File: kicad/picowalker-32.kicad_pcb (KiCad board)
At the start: 2 copper layers, 44.1 x 51 mm, 50 parts, among them IC1 TFBS4711-TT1, J1 DBG_HDR, J2 PROGRAM_HDR, J5 USB_C_Receptacle_USB2.0, SW1 SW_Push, SW2 SW_Push, SW3 SW_Push, SW5 BOOTSEL, U1 MCP73871, U10 MCP1700x-180xxTT, U11 USBLC6-2P6, U12 STM32U535CET6-modified, U2 M95512-DWDW4TP_K, U3 BMA400, U4 W25Q128JVS

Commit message: Change schematic MCU pinouts
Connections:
- U12 pad 10: TXDIR -> WKUP
- U12 pad 11: RXDIR -> ACCEL_INT1
- U12 pad 12: SCREEN_CSB -> DBG_TX
- U12 pad 14: SOUND_SRC -> SCREEN_CSB
- U12 pad 15: unconnected-(U12-PA5-Pad15) -> SOUND_SRC
- U12 pad 20: WKUP -> SCREEN_RST
- U12 pad 21: unconnected-(U12-PB10-Pad21) -> DBG_RX
- U12 pad 25: unconnected-(U12-PB12-Pad25) -> TP_INT
- U12 pad 30: DBG_TX -> TXDIR
- U12 pad 31: DBG_RX -> RXDIR
- U12 pad 39: SWO -> BSTAT2
- U12 pad 45: /stm32u5/~{BAT_LO} -> ~{PG}
- U12 pad 46: unconnected-(U12-PB9-Pad46) -> BSTAT1

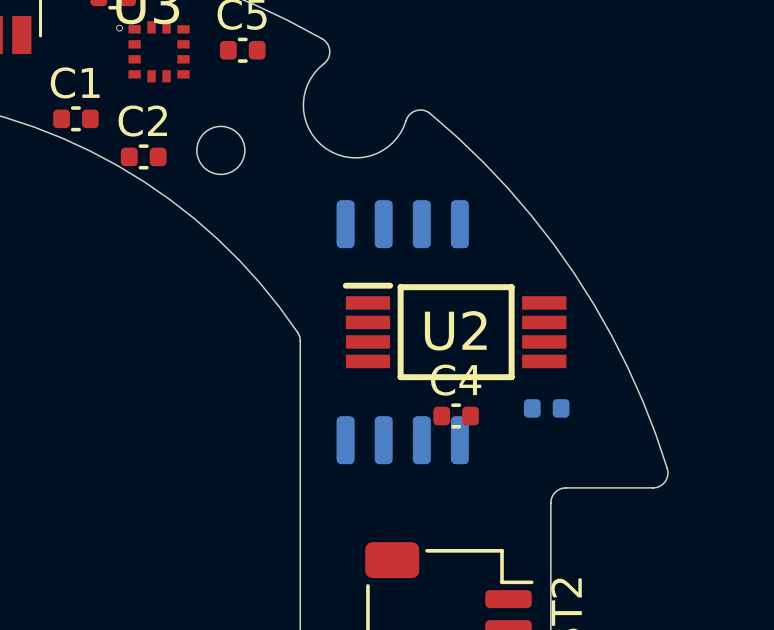
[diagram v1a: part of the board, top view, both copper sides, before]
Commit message: comments about power, changed eeprom and flash packages
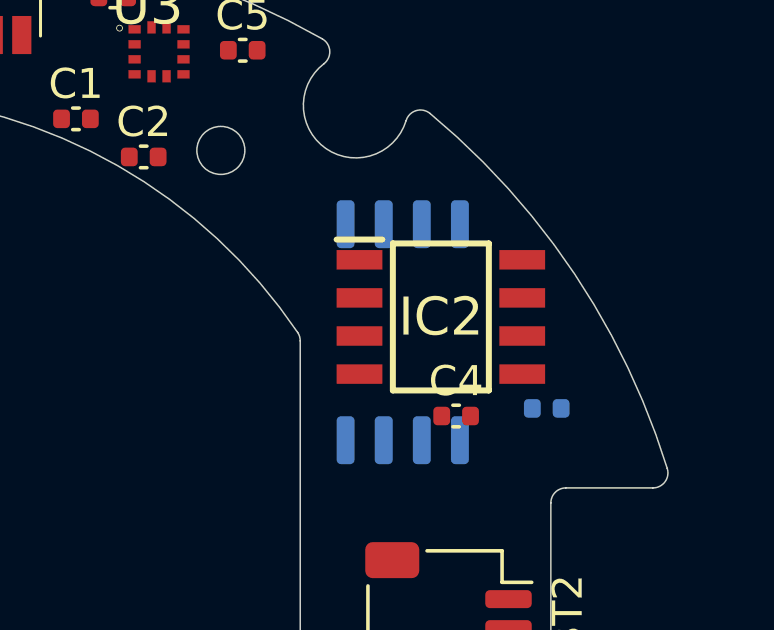
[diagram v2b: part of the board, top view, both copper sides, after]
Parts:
- removed U2: M95512-DWDW4TP_K, Samacsys_Parts:SOP65P640X120-8N
- added IC2: M95512-DRMN8TP_K, SamacSys_Parts:SOIC127P600X175-8N, F.Cu at (116.3, 68.8)
- C26: value C -> 4.7uF
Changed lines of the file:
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@@
         (effects (font (size 1 1) (thickness 0.15)))
     )
-    (fp_text value "C" (at 0 1.16) (layer "F.Fab")
+    (fp_text value "4.7uF" (at 0 1.16) (layer "F.Fab")
         (effects (font (size 1 1) (thickness 0.15)))
     )
@@
     )
   )
-  (footprint "Samacsys_Parts:SOP65P640X120-8N" (layer "F.Cu")
-    (at 116.84 69.342)
-    (descr "M95512-DWDW4TP/K")
-    (tags "Integrated Circuit")
-    (property "Description" "Automotive 512 Kbit SPI bus EEPROM with high speed clock")
-    (property "Height" "1.2")
-    (property "Manufacturer_Name" "STMicroelectronics")
-    (property "Manufacturer_Part_Number" "M95512-DWDW4TP/K")
-    (property "Mouser Part Number" "511-M95512-DWDW4TP/K")
-    (property "Mouser Price/Stock" "https://www.mouser.co.uk/ProductDetail/STMicroelectronics/M95512-DWDW4TP-K?qs=gNDSiZmRJS8kMWQ2whknqA%3D%3D")
-    (property "Sheetfile" "picowalker-32.kicad_sch")
-    (property "Sheetname" "")
-    (property "ki_description" "Automotive 512 Kbit SPI bus EEPROM with high speed clock")
-    (attr smd)
-    (fp_text reference "U2" (at 0 0) (layer "F.SilkS")
-        (effects (font (size 1.27 1.27) (thickness 0.254)))
-    )
-    (fp_text value "M95512-DWDW4TP_K" (at 0 0) (layer "F.SilkS") hide
-        (effects (font (size 1.27 1.27) (thickness 0.254)))
-    )
-    (fp_text user "${REFERENCE}" (at 0 0) (layer "F.Fab")
-        (effects (font (size 1.27 1.27) (thickness 0.254)))
-    )
-    (fp_line (start -3.675 -1.55) (end -2.2 -1.55)
-      (stroke (width 0.2) (type solid)) (layer "F.SilkS"))
-    (fp_line (start -1.85 -1.5) (end 1.85 -1.5)
-      (stroke (width 0.2) (type solid)) (layer "F.SilkS"))
-    (fp_line (start -1.85 1.5) (end -1.85 -1.5)
-      (stroke (width 0.2) (type solid)) (layer "F.SilkS"))
-    (fp_line (start 1.85 -1.5) (end 1.85 1.5)
-      (stroke (width 0.2) (type solid)) (layer "F.SilkS"))
-    (fp_line (start 1.85 1.5) (end -1.85 1.5)
-      (stroke (width 0.2) (type solid)) (layer "F.SilkS"))
-    (fp_line (start -3.925 -1.8) (end 3.925 -1.8)
-      (stroke (width 0.05) (type solid)) (layer "F.CrtYd"))
-    (fp_line (start -3.925 1.8) (end -3.925 -1.8)
-      (stroke (width 0.05) (type solid)) (layer "F.CrtYd"))
-    (fp_line (start 3.925 -1.8) (end 3.925 1.8)
-      (stroke (width 0.05) (type solid)) (layer "F.CrtYd"))
-    (fp_line (start 3.925 1.8) (end -3.925 1.8)
-      (stroke (width 0.05) (type solid)) (layer "F.CrtYd"))
-    (fp_line (start -2.2 -1.5) (end 2.2 -1.5)
-      (stroke (width 0.1) (type solid)) (layer "F.Fab"))
-    (fp_line (start -2.2 -0.85) (end -1.55 -1.5)
-      (stroke (width 0.1) (type solid)) (layer "F.Fab"))
-    (fp_line (start -2.2 1.5) (end -2.2 -1.5)
-      (stroke (width 0.1) (type solid)) (layer "F.Fab"))
-    (fp_line (start 2.2 -1.5) (end 2.2 1.5)
-      (stroke (width 0.1) (type solid)) (layer "F.Fab"))
-    (fp_line (start 2.2 1.5) (end -2.2 1.5)
-      (stroke (width 0.1) (type solid)) (layer "F.Fab"))
-    (pad "1" smd rect (at -2.938 -0.975 90) (size 0.45 1.475) (layers "F.Cu" "F.Paste" "F.Mask")
-      (net 46 "EEPROM_CSB") (pinfunction "~{S}") (pintype "passive"))
-    (pad "2" smd rect (at -2.938 -0.325 90) (size 0.45 1.475) (layers "F.Cu" "F.Paste" "F.Mask")
-      (net 44 "MISO") (pinfunction "Q") (pintype "passive"))
-    (pad "3" smd rect (at -2.938 0.325 90) (size 0.45 1.475) (layers "F.Cu" "F.Paste" "F.Mask")
-      (net 5 "PWR") (pinfunction "~{W}") (pintype "passive"))
-    (pad "4" smd rect (at -2.938 0.975 90) (size 0.45 1.475) (layers "F.Cu" "F.Paste" "F.Mask")
-      (net 2 "GND") (pinfunction "VSS") (pintype "passive"))
-    (pad "5" smd rect (at 2.938 0.975 90) (size 0.45 1.475) (layers "F.Cu" "F.Paste" "F.Mask")
-      (net 45 "MOSI") (pinfunction "D") (pintype "passive"))
-    (pad "6" smd rect (at 2.938 0.325 90) (size 0.45 1.475) (layers "F.Cu" "F.Paste" "F.Mask")
-      (net 43 "SCK") (pinfunction "C") (pintype "passive"))
-    (pad "7" smd rect (at 2.938 -0.325 90) (size 0.45 1.475) (layers "F.Cu" "F.Paste" "F.Mask")
-      (net 5 "PWR") (pinfunction "~{HOLD}") (pintype "passive"))
-    (pad "8" smd rect (at 2.938 -0.975 90) (size 0.45 1.475) (layers "F.Cu" "F.Paste" "F.Mask")
-      (net 5 "PWR") (pinfunction "VCC") (pintype "passive"))
-    (model "C:\\Users\\Callum\\SamacsysParts\\SamacSys_Parts.3dshapes\\M95512-DWDW4TP_K.stp"
-      (offset (xyz 0 0 0))
-      (scale (xyz 1 1 1))
-      (rotate (xyz 0 0 0))
-    )
-  )
   (footprint "Capacitor_SMD:C_0402_1005Metric" (layer "F.Cu")
     (at 102.616 87.376)
@@
       (offset (xyz 0 0 0))
       (scale (xyz 1 1 1))
+      (rotate (xyz 0 0 0))
+    )
+  )
+  (footprint "SamacSys_Parts:SOIC127P600X175-8N" (layer "F.Cu")
+    (at 116.332 68.834)
+    (descr "SO8N (150 mils width)")
+    (tags "Integrated Circuit")
+    (property "Height" "1.75")
+    (property "Manufacturer_Name" "STMicroelectronics")
+    (property "Manufacturer_Part_Number" "M95512-DRMN8TP/K")
+    (property "Mouser Part Number" "511-M95512-DRMN8TP/K")
+    (property "Mouser Price/Stock" "https://www.mouser.co.uk/ProductDetail/STMicroelectronics/M95512-DRMN8TP-K?qs=Ng9CY5lTJpjKk8df9nXMMQ%3D%3D")
+    (property "Sheetfile" "picowalker-32.kicad_sch")
+    (property "Sheetname" "")
+    (property "ki_description" "STMICROELECTRONICS - M95512-DRMN8TP/K - EEPROM, 512 Kbit, 64K x 8bit, Serial SPI, 16 MHz, SOIC, 8 Pins")
+    (attr smd)
+    (fp_text reference "IC2" (at 0 0) (layer "F.SilkS")
+        (effects (font (size 1.27 1.27) (thickness 0.254)))
+    )
+    (fp_text value "M95512-DRMN8TP_K" (at 0 0) (layer "F.SilkS") hide
+        (effects (font (size 1.27 1.27) (thickness 0.254)))
+    )
+    (fp_text user "${REFERENCE}" (at 0 0) (layer "F.Fab")
+        (effects (font (size 1.27 1.27) (thickness 0.254)))
+    )
+    (fp_line (start -3.475 -2.58) (end -1.95 -2.58)
+      (stroke (width 0.2) (type solid)) (layer "F.SilkS"))
+    (fp_line (start -1.6 -2.45) (end 1.6 -2.45)
+      (stroke (width 0.2) (type solid)) (layer "F.SilkS"))
+    (fp_line (start -1.6 2.45) (end -1.6 -2.45)
+      (stroke (width 0.2) (type solid)) (layer "F.SilkS"))
+    (fp_line (start 1.6 -2.45) (end 1.6 2.45)
+      (stroke (width 0.2) (type solid)) (layer "F.SilkS"))
+    (fp_line (start 1.6 2.45) (end -1.6 2.45)
+      (stroke (width 0.2) (type solid)) (layer "F.SilkS"))
+    (fp_line (start -3.725 -2.75) (end 3.725 -2.75)
+      (stroke (width 0.05) (type solid)) (layer "F.CrtYd"))
+    (fp_line (start -3.725 2.75) (end -3.725 -2.75)
+      (stroke (width 0.05) (type solid)) (layer "F.CrtYd"))
+    (fp_line (start 3.725 -2.75) (end 3.725 2.75)
+      (stroke (width 0.05) (type solid)) (layer "F.CrtYd"))
+    (fp_line (start 3.725 2.75) (end -3.725 2.75)
+      (stroke (width 0.05) (type solid)) (layer "F.CrtYd"))
+    (fp_line (start -1.95 -2.45) (end 1.95 -2.45)
+      (stroke (width 0.1) (type solid)) (layer "F.Fab"))
+    (fp_line (start -1.95 -1.18) (end -0.68 -2.45)
+      (stroke (width 0.1) (type solid)) (layer "F.Fab"))
+    (fp_line (start -1.95 2.45) (end -1.95 -2.45)
+      (stroke (width 0.1) (type solid)) (layer "F.Fab"))
+    (fp_line (start 1.95 -2.45) (end 1.95 2.45)
+      (stroke (width 0.1) (type solid)) (layer "F.Fab"))
+    (fp_line (start 1.95 2.45) (end -1.95 2.45)
+      (stroke (width 0.1) (type solid)) (layer "F.Fab"))
+    (pad "1" smd rect (at -2.712 -1.905 90) (size 0.65 1.525) (layers "F.Cu" "F.Paste" "F.Mask")
+      (net 46 "EEPROM_CSB") (pinfunction "~{S}") (pintype "passive"))
+    (pad "2" smd rect (at -2.712 -0.635 90) (size 0.65 1.525) (layers "F.Cu" "F.Paste" "F.Mask")
+      (net 44 "MISO") (pinfunction "Q") (pintype "passive"))
+    (pad "3" smd rect (at -2.712 0.635 90) (size 0.65 1.525) (layers "F.Cu" "F.Paste" "F.Mask")
+      (net 5 "PWR") (pinfunction "~{W}") (pintype "passive"))
+    (pad "4" smd rect (at -2.712 1.905 90) (size 0.65 1.525) (layers "F.Cu" "F.Paste" "F.Mask")
+      (net 2 "GND") (pinfunction "VSS") (pintype "passive"))
+    (pad "5" smd rect (at 2.712 1.905 90) (size 0.65 1.525) (layers "F.Cu" "F.Paste" "F.Mask")
+      (net 45 "MOSI") (pinfunction "D") (pintype "passive"))
+    (pad "6" smd rect (at 2.712 0.635 90) (size 0.65 1.525) (layers "F.Cu" "F.Paste" "F.Mask")
+      (net 43 "SCK") (pinfunction "C") (pintype "passive"))
+    (pad "7" smd rect (at 2.712 -0.635 90) (size 0.65 1.525) (layers "F.Cu" "F.Paste" "F.Mask")
+      (net 5 "PWR") (pinfunction "~{HOLD}") (pintype "passive"))
+    (pad "8" smd rect (at 2.712 -1.905 90) (size 0.65 1.525) (layers "F.Cu" "F.Paste" "F.Mask")
+      (net 5 "PWR") (pinfunction "VCC") (pintype "passive"))
+    (model "C:\\Users\\cmcgregor\\Documents\\LibraryLoader\\SamacSys_Parts.3dshapes\\M95512-DRMN8TP_K.stp"
+      (offset (xyz 0 0 0))
+      (scale (xyz 1 1 1))
